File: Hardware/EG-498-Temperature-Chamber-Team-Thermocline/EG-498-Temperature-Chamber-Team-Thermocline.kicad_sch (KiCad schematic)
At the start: 0 parts

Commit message: Add Inital IDC connectors
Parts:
- added J1: HMI_Daughter_Connector, Connector_IDC:IDC-Header_2x10_P2.54mm_Vertical, symbol Connector_Generic:Conn_02x10_Counter_Clockwise
- added J2: Conn_02x10_Counter_Clockwise, Connector_IDC:IDC-Header_2x10_P2.54mm_Vertical, symbol Connector_Generic:Conn_02x10_Counter_Clockwise
- added J3: Disp_Connector, Connector_PinHeader_2.00mm:PinHeader_1x16_P2.00mm_Horizontal, symbol Connector:Conn_01x16_Pin
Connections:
- new net: J1.1 (Pin_1), J3.1 (Pin_1)
- new net: J1.10 (Pin_10), J3.10 (Pin_10)
- new net: J1.11 (Pin_11), J3.11 (Pin_11)
- new net: J1.12 (Pin_12), J3.12 (Pin_12)
- new net: J1.13 (Pin_13), J3.13 (Pin_13)
- new net: J1.14 (Pin_14), J3.14 (Pin_14)
- new net: J1.15 (Pin_15), J3.15 (Pin_15)
- new net: J1.16 (Pin_16), J3.16 (Pin_16)
- new net: J1.2 (Pin_2), J3.2 (Pin_2)
- new net: J1.3 (Pin_3), J3.3 (Pin_3)
- new net: J1.4 (Pin_4), J3.4 (Pin_4)
- new net: J1.5 (Pin_5), J3.5 (Pin_5)
- new net: J1.6 (Pin_6), J3.6 (Pin_6)
- new net: J1.7 (Pin_7), J3.7 (Pin_7)
- new net: J1.8 (Pin_8), J3.8 (Pin_8)
- new net: J1.9 (Pin_9), J3.9 (Pin_9)
- no-connect marks 0 -> 4
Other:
- note added: "HMI Ribbon Interface"

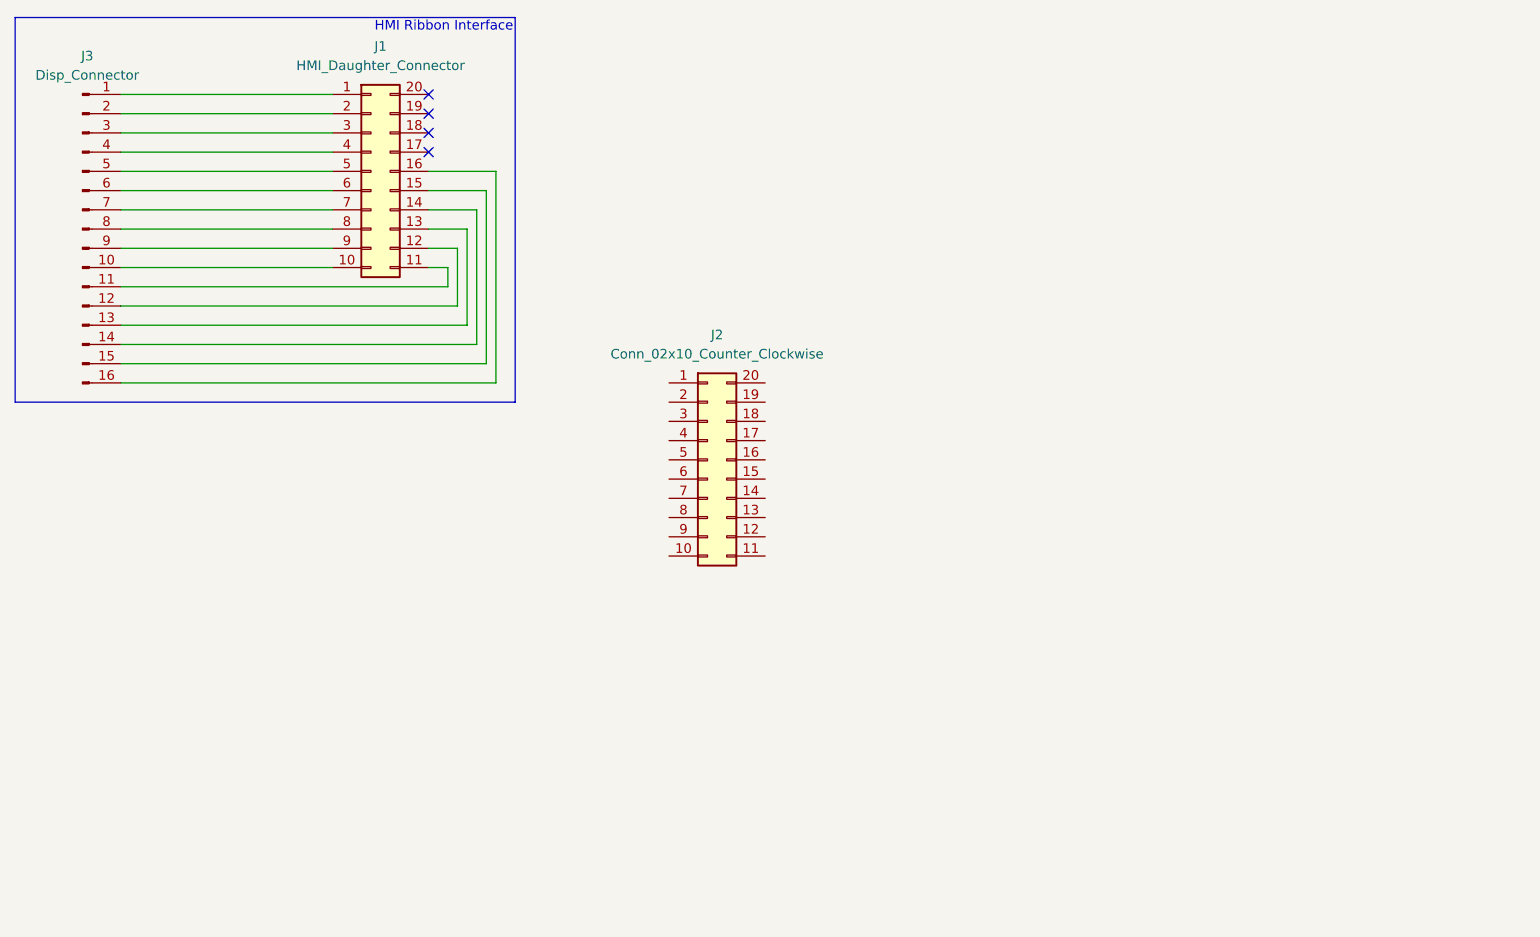
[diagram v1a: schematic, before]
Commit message: Add basic outline for inital connector adapter and kicad libs
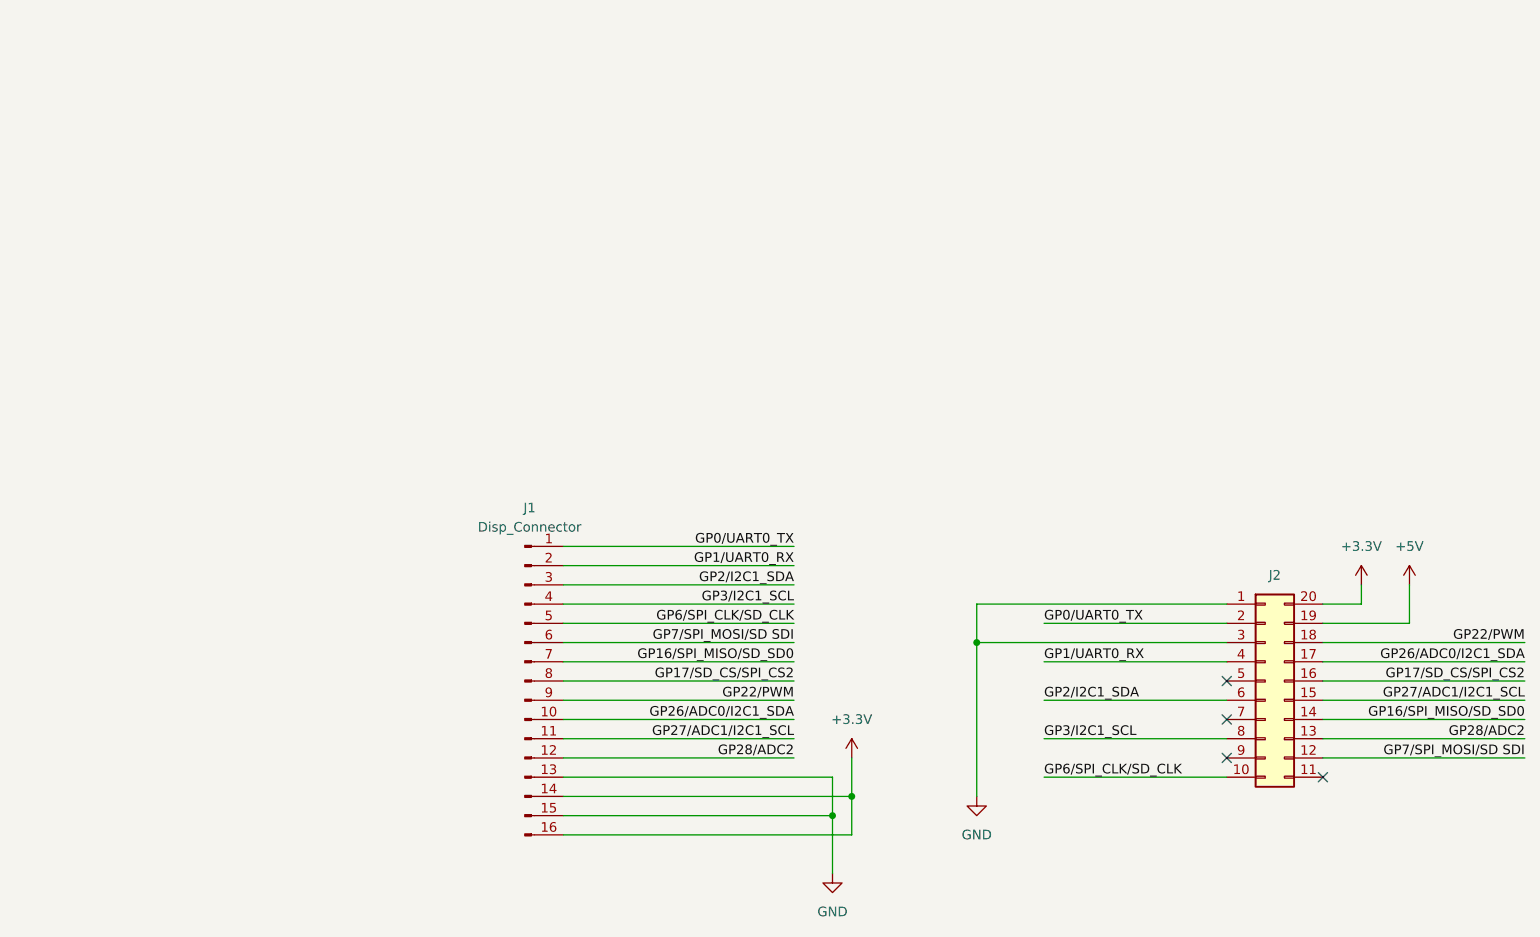
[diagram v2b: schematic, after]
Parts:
- removed J2: Conn_02x10_Counter_Clockwise, Connector_IDC:IDC-Header_2x10_P2.54mm_Vertical, symbol Connector_Generic:Conn_02x10_Counter_Clockwise
- J1: renamed from J3; footprint Connector_PinHeader_2.00mm:PinHeader_1x16_P2.00mm_Horizontal -> Connector_PinHeader_2.54mm:PinHeader_1x16_P2.54mm_Vertical
- renumbered J1 to J2
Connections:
- net GND: now reaches J2.1 (Pin_1)
- net GND: now also J1.13 (Pin_13), J1.15 (Pin_15), J2.3 (Pin_3); no longer J1.1 (Pin_1)
- net GP26/ADC0/I2C1_SDA: now reaches J1.10 (Pin_10)
- net GP26/ADC0/I2C1_SDA: now also J2.17 (Pin_17); no longer J2.10 (Pin_10)
- net at J2.11 (Pin_11): no longer J1.11 (Pin_11)
- net GP28/ADC2: now reaches J1.12 (Pin_12)
- net GP28/ADC2: now also J2.13 (Pin_13); no longer J2.12 (Pin_12)
- net +3.3V: now reaches J1.14 (Pin_14)
- net +3.3V: now also J1.16 (Pin_16), J2.20 (Pin_20); no longer J2.14 (Pin_14)
- net GP27/ADC1/I2C1_SCL: now reaches J2.15 (Pin_15)
- net GP27/ADC1/I2C1_SCL: now also J1.11 (Pin_11); no longer J1.15 (Pin_15)
- net GP17/SD_CS/SPI_CS2: now reaches J2.16 (Pin_16)
- net GP17/SD_CS/SPI_CS2: now also J1.8 (Pin_8); no longer J1.16 (Pin_16)
- net GP0/UART0_TX: now reaches J2.2 (Pin_2)
- net GP0/UART0_TX: now also J1.1 (Pin_1); no longer J1.2 (Pin_2)
- net GP2/I2C1_SDA: now reaches J1.3 (Pin_3)
- net GP2/I2C1_SDA: now also J2.6 (Pin_6); no longer J2.3 (Pin_3)
- net GP1/UART0_RX: now reaches J2.4 (Pin_4)
- net GP1/UART0_RX: now also J1.2 (Pin_2); no longer J1.4 (Pin_4)
- net at J2.5 (Pin_5): no longer J1.5 (Pin_5)
- net GP7/SPI_MOSI/SD SDI: now reaches J1.6 (Pin_6)
- net GP7/SPI_MOSI/SD SDI: now also J2.12 (Pin_12); no longer J2.6 (Pin_6)
- net at J2.7 (Pin_7): no longer J1.7 (Pin_7)
- net GP3/I2C1_SCL: now reaches J2.8 (Pin_8)
- net GP3/I2C1_SCL: now also J1.4 (Pin_4); no longer J1.8 (Pin_8)
- net at J2.9 (Pin_9): no longer J1.9 (Pin_9)
- net GP22/PWM: now reaches J2.18 (Pin_18)
- net GP22/PWM: now also J1.9 (Pin_9)
- net +5V: now reaches J2.19 (Pin_19)
- new net GP16/SPI_MISO/SD_SD0: J1.7 (Pin_7), J2.14 (Pin_14)
- new net GP6/SPI_CLK/SD_CLK: J1.5 (Pin_5), J2.10 (Pin_10)
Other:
- note removed: "HMI Ribbon Interface"
- moved on the sheet: J1, J2
